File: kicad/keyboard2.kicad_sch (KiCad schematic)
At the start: 162 parts, among them J1 Conn_02x06_Odd_Even, J2 Conn_01x12, J3 Conn_01x12_MountingPin, J4 USB_B_Mini, J5 Conn_02x03_Odd_Even, SW1 SW_Push, SW10 SW_Push, SW11 SW_Push, SW12 SW_Push, SW13 SW_Push, SW14 SW_Push, SW15 SW_Push, SW16 SW_Push, SW17 SW_Push, SW18 SW_Push, SW19 SW_Push, SW2 SW_Push, SW20 SW_Push, SW21 SW_Push, SW22 SW_Push, SW23 SW_Push, SW24 SW_Push, SW25 SW_Push, SW26 SW_Push, SW27 SW_Push, SW28 SW_Push, SW29 SW_Push, SW3 SW_Push, SW30 SW_Push, SW31 SW_Push, SW32 SW_Push, SW33 SW_Push, SW34 SW_Push, SW35 SW_Push, SW36 SW_Push, SW37 SW_Push, SW38 SW_Push, SW39 SW_Push, SW4 SW_Push, SW40 SW_Push, SW41 SW_Push, SW42 SW_Push, SW43 SW_Push, SW44 SW_Push, SW45 SW_Push, SW46 SW_Push, SW47 SW_Push, SW48 SW_Push, SW49 SW_Push, SW5 SW_Push, SW50 SW_Push, SW51 SW_Push, SW52 SW_Push, SW53 SW_Push, SW54 SW_Push, SW55 SW_Push, SW56 SW_Push, SW57 SW_Push, SW58 SW_Push, SW59 SW_Push, SW6 SW_Push, SW60 SW_Push, SW61 SW_Push, SW62 SW_Push, SW63 SW_Push, SW64 SW_Push, SW65 SW_Push, SW66 SW_Push, SW67 SW_Push, SW68 SW_Push, SW7 SW_Push, SW8 SW_Push, SW9 SW_Push, U1 74HC138, U2 74HC138, U3 ATmega16U4-A, Y1 Crystal

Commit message: Revision B:
- fix wrong space size (6.5u -> 6.25u),
- fix wrong right shift size (2u -> 1.75u),
- fix wrong placement of space stabilizer,
- fix J1 being mirrored against IDC-12 connector,
- change diodes footprint (hand soldering version has way too big pads),
- reroute.
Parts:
- D1, D10, D11, D12, D13, D14, D15, D16, D17, D18, D19, D2, D20, D21, D22, D23, D24, D25, D26, D27, D28, D29, D3, D30, D31, D32, D33, D34, D35, D36, D37, D38, D39, D4, D40, D41, D42, D43, D44, D45, D46, D47, D48, D49, D5, D50, D51, D52, D53, D54, D55, D56, D57, D58, D59, D6, D60, D61, D62, D63, D64, D65, D66, D67, D68, D7, D8, D9: footprint Diode_SMD:D_MiniMELF_Handsoldering -> Diode_SMD:D_MiniMELF
- J1: footprint Connector_PinSocket_2.54mm:PinSocket_2x06_P2.54mm_Vertical -> Connector_IDC:IDC-Header_2x06_P2.54mm_Vertical
- SW1, SW10, SW11, SW12, SW13, SW15, SW17, SW18, SW19, SW2, SW20, SW21, SW22, SW23, SW24, SW25, SW26, SW27, SW28, SW3, SW30, SW32, SW33, SW34, SW35, SW36, SW37, SW38, SW39, SW4, SW40, SW41, SW42, SW44, SW46, SW47, SW48, SW49, SW5, SW50, SW51, SW52, SW53, SW54, SW55, SW57, SW58, SW6, SW63, SW64, SW65, SW66, SW67, SW68, SW7, SW8, SW9: footprint PCM_Switch_Keyboard_Cherry_MX:SW_Cherry_MX_PCB_1.00u -> Button_Switch_Keyboard:SW_Cherry_MX_1.00u_PCB
- SW14: footprint PCM_Switch_Keyboard_Cherry_MX:SW_Cherry_MX_PCB_2.25u -> Button_Switch_Keyboard:SW_Cherry_MX_2.00u_PCB
- SW16: footprint PCM_Switch_Keyboard_Cherry_MX:SW_Cherry_MX_PCB_1.50u -> Button_Switch_Keyboard:SW_Cherry_MX_1.50u_PCB
- SW29: footprint PCM_Switch_Keyboard_Cherry_MX:SW_Cherry_MX_PCB_1.75u -> Button_Switch_Keyboard:SW_Cherry_MX_1.50u_PCB
- SW31: footprint PCM_Switch_Keyboard_Cherry_MX:SW_Cherry_MX_PCB_1.75u -> Button_Switch_Keyboard:SW_Cherry_MX_1.75u_PCB
- SW43: footprint PCM_Switch_Keyboard_Cherry_MX:SW_Cherry_MX_PCB_2.50u -> Button_Switch_Keyboard:SW_Cherry_MX_2.25u_PCB
- SW45: footprint PCM_Switch_Keyboard_Cherry_MX:SW_Cherry_MX_PCB_2.25u -> Button_Switch_Keyboard:SW_Cherry_MX_2.25u_PCB
- SW56: footprint PCM_Switch_Keyboard_Cherry_MX:SW_Cherry_MX_PCB_2.00u -> Button_Switch_Keyboard:SW_Cherry_MX_1.75u_PCB
- SW59, SW60, SW61: footprint PCM_Switch_Keyboard_Cherry_MX:SW_Cherry_MX_PCB_1.25u -> Button_Switch_Keyboard:SW_Cherry_MX_1.25u_PCB
- SW62: footprint PCM_Switch_Keyboard_Cherry_MX:SW_Cherry_MX_PCB_6.50u -> Button_Switch_Keyboard:SW_Cherry_MX_6.25u_PCB

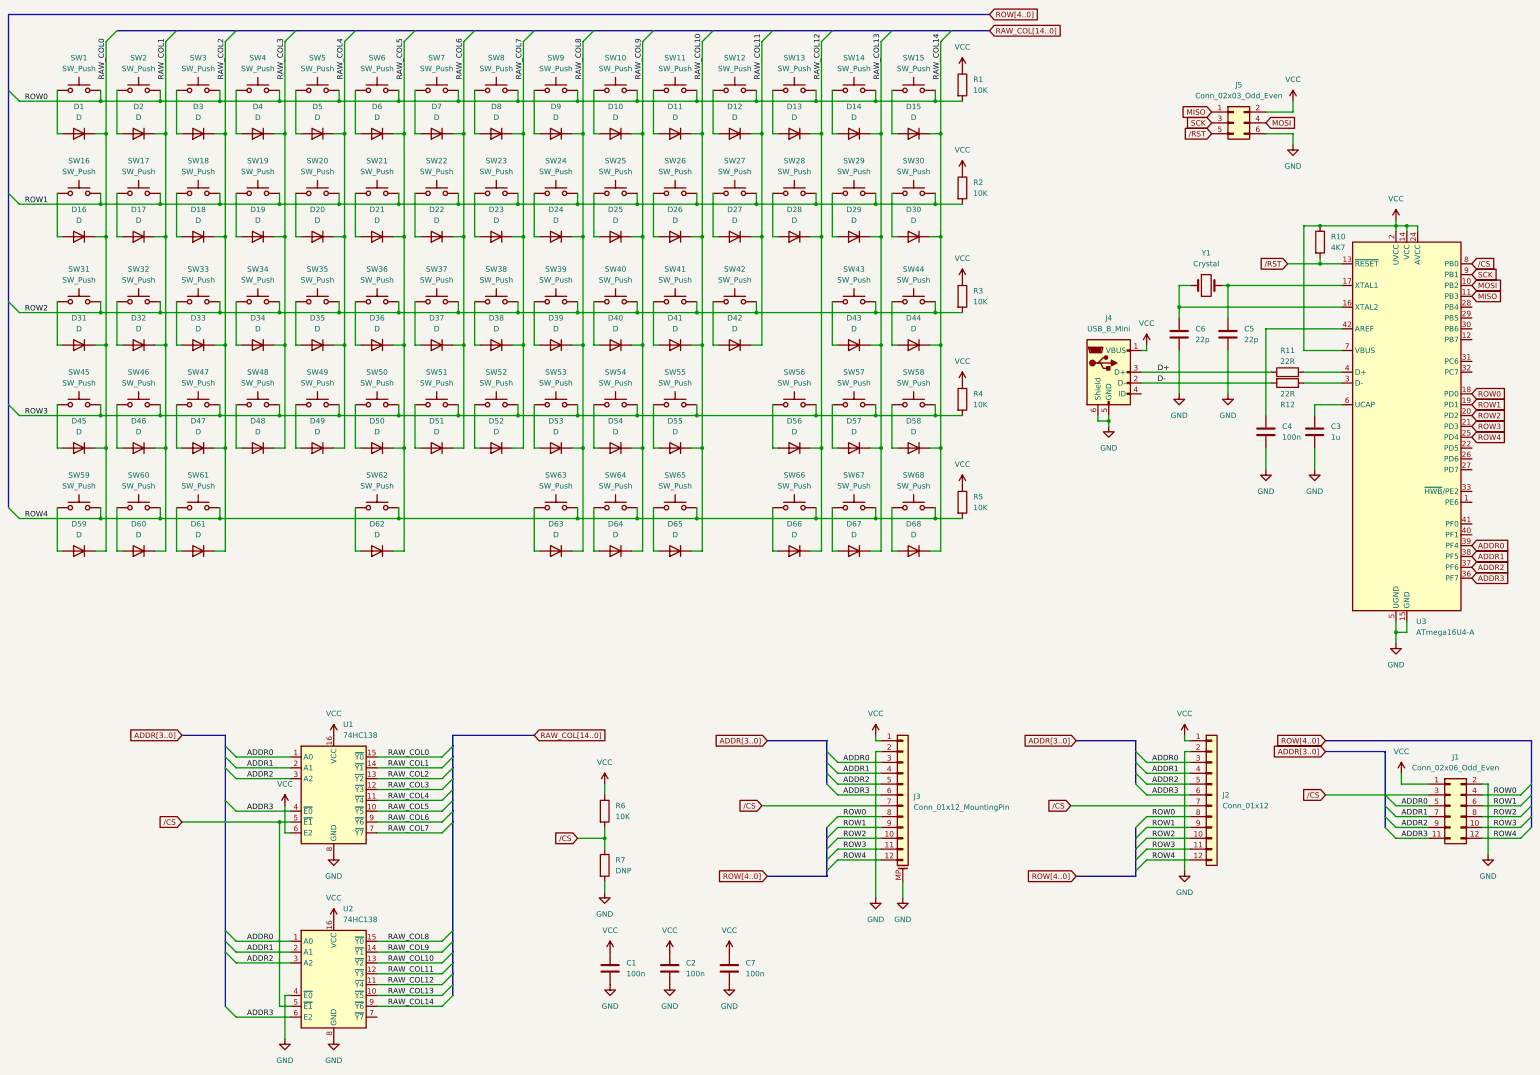
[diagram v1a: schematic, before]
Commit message: Add mini version
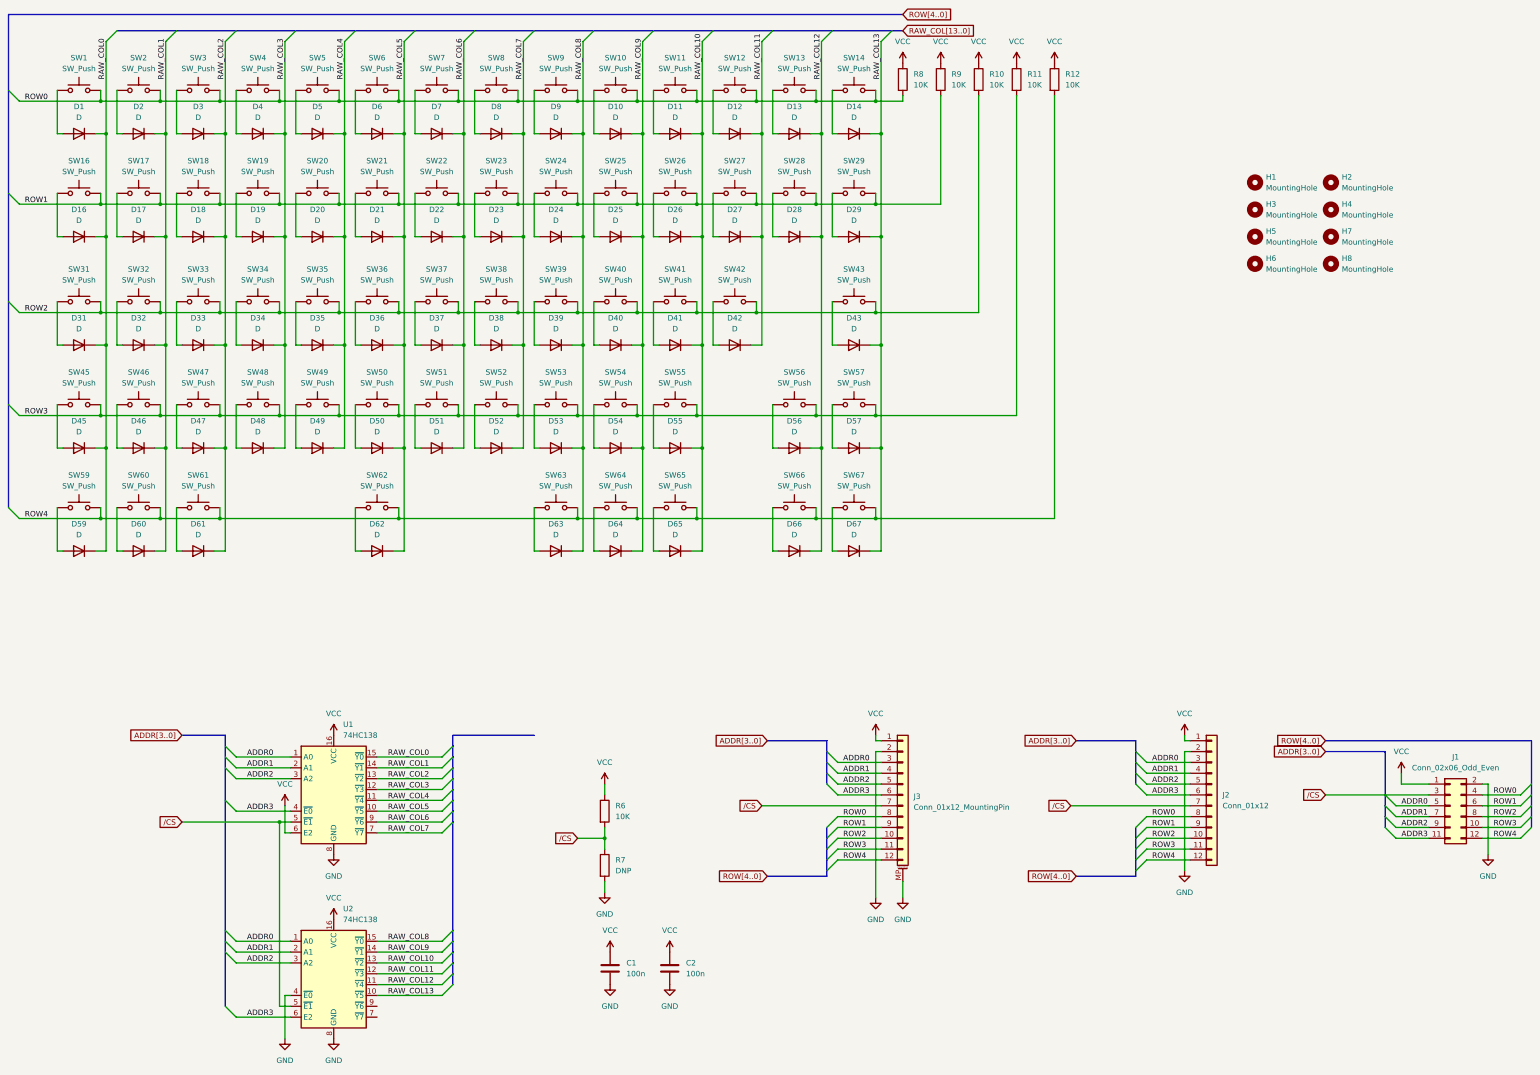
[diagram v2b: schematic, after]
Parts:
- removed C3: 1u, Capacitor_SMD:C_0805_2012Metric_Pad1.18x1.45mm_HandSolder, symbol Device:C
- removed C4, C7: 100n, Capacitor_SMD:C_0805_2012Metric_Pad1.18x1.45mm_HandSolder, symbol Device:C
- removed C5, C6: 22p, Capacitor_SMD:C_0805_2012Metric_Pad1.18x1.45mm_HandSolder, symbol Device:C
- removed D15, D30, D44, D58, D68: D, Diode_SMD:D_MiniMELF, symbol Device:D
- removed J4: USB_B_Mini, Connector_USB:USB_Mini-B_Wuerth_65100516121_Horizontal, symbol Connector:USB_B_Mini
- removed J5: Conn_02x03_Odd_Even, Connector_PinHeader_2.54mm:PinHeader_2x03_P2.54mm_Vertical, symbol Connector_Generic:Conn_02x03_Odd_Even
- removed R1, R2, R3, R4, R5: 10K, Resistor_SMD:R_0805_2012Metric_Pad1.20x1.40mm_HandSolder, symbol Device:R
- removed SW15, SW30, SW44, SW58, SW68: SW_Push, Button_Switch_Keyboard:SW_Cherry_MX_1.00u_PCB, symbol Switch:SW_Push
- removed U3: ATmega16U4-A, Package_QFP:TQFP-44_10x10mm_P0.8mm, symbol MCU_Microchip_ATmega:ATmega16U4-A
- removed Y1: Crystal, Crystal:Crystal_HC49-4H_Vertical, symbol Device:Crystal
- added H1, H2, H3, H4, H5, H6, H7, H8: MountingHole, MountingHole:MountingHole_2.7mm_M2.5_Pad_Via, symbol Mechanical:MountingHole
- added R8, R9: 10K, Resistor_SMD:R_0805_2012Metric_Pad1.20x1.40mm_HandSolder, symbol Device:R
- R10: value 4K7 -> 10K
- R11, R12: value 22R -> 10K
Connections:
- net D+ is gone; now on net VCC: R11.1
- net D- is gone; now on net ROW4: R12.2
- net /RST is gone; now on net ROW2: R10.2
- net ROW0: now also R8.2
- net ROW1: now also R9.2
- net ROW3: now also R11.2
- net VCC: now also R12.1, R8.1, R9.1
- net RAW_COL14: no longer names the net of U2.9 (~{Y6})
